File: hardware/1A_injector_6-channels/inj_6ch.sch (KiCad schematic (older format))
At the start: 35 parts, among them P401 HEADER_10X2, P402 CONN_2, P403 CONN_3, P404 CONN_2, P405 CONN_3, P406 HEADER_10X2, Q401 OVP_DRIVER, Q402 OVP_DRIVER, Q403 OVP_DRIVER, Q404 OVP_DRIVER, Q405 OVP_DRIVER, Q406 OVP_DRIVER

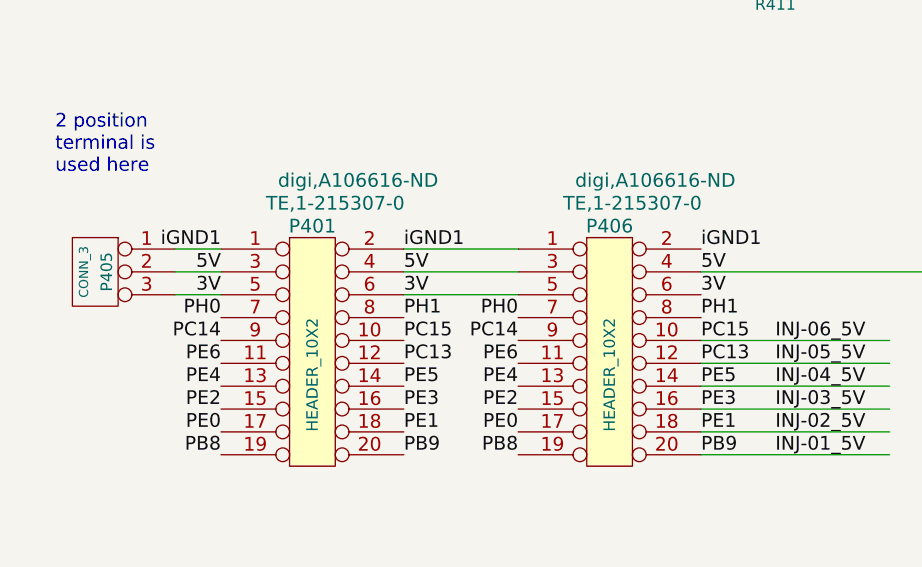
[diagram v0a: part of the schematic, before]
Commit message: 3v > 3.3v
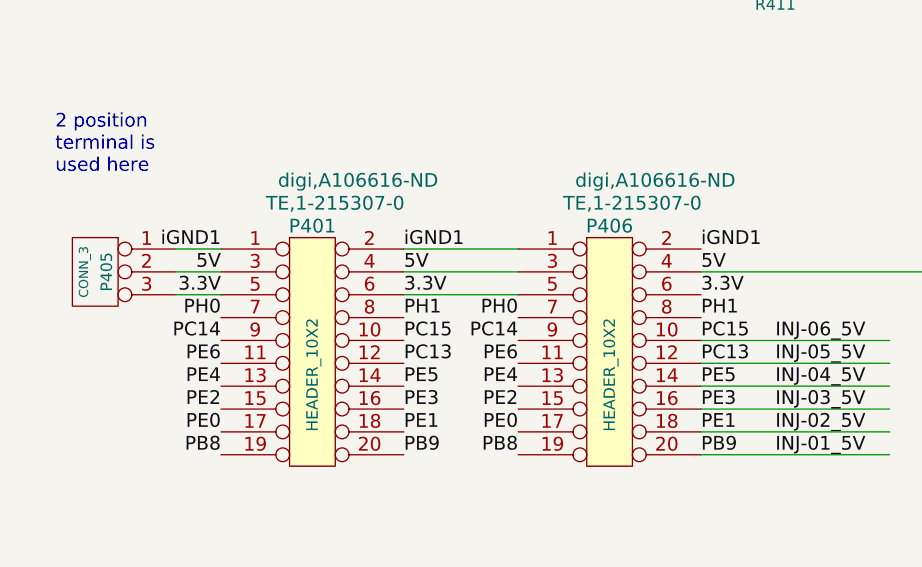
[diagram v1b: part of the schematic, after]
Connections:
- net labels added: 3.3V
- net labels removed: 3V
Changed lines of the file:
@@
 Sheet 1 1
 Title "6 Channel Injector"
-Date "30 dec 2013"
+Date "19 jan 2014"
 Rev "A-6"
 Comp "http://code.google.com/p/daecu/"
@@
 5V
 Text Label 1275 6575 2    60   ~ 0
-3V
+3.3V
 Text Label 2075 6475 0    60   ~ 0
 5V
 Text Label 2075 6575 0    60   ~ 0
-3V
+3.3V
 Text Label 1275 6775 2    60   ~ 0
 PC14
@@
 5V
 Text Label 3375 6575 0    60   ~ 0
-3V
+3.3V
 Text Label 2575 6775 2    60   ~ 0
 PC14
